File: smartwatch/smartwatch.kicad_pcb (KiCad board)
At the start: 4 copper layers, 40.1 x 29.7 mm, 35 parts, among them J1 BAT_CON, J2 DC_CON, J3 PROG_INT, J4 Screen, J5 Touch, J6 Power, SW1 SW_Push, U1 ESP32-WROVER-E, U2 MCP73831-5-OT, U3 MPU-6050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

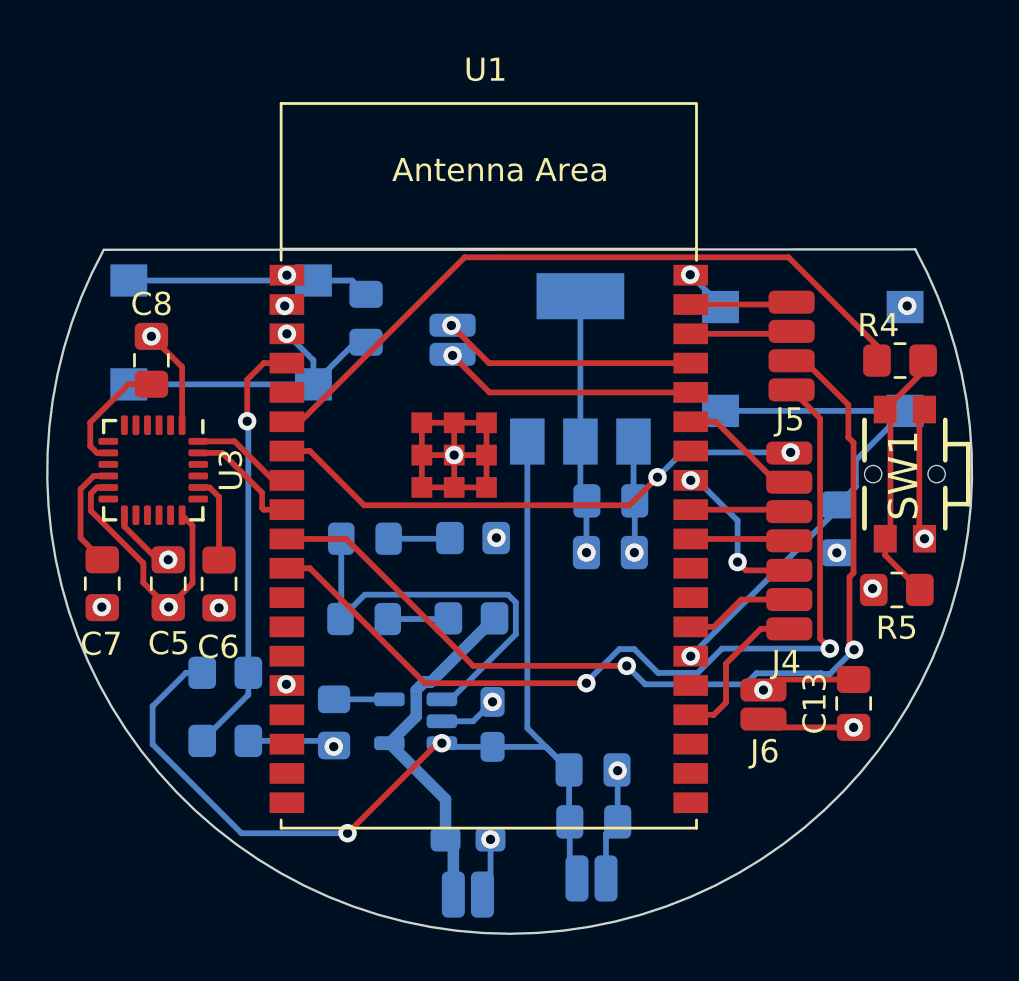
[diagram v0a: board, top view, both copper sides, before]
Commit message: added missing pullups
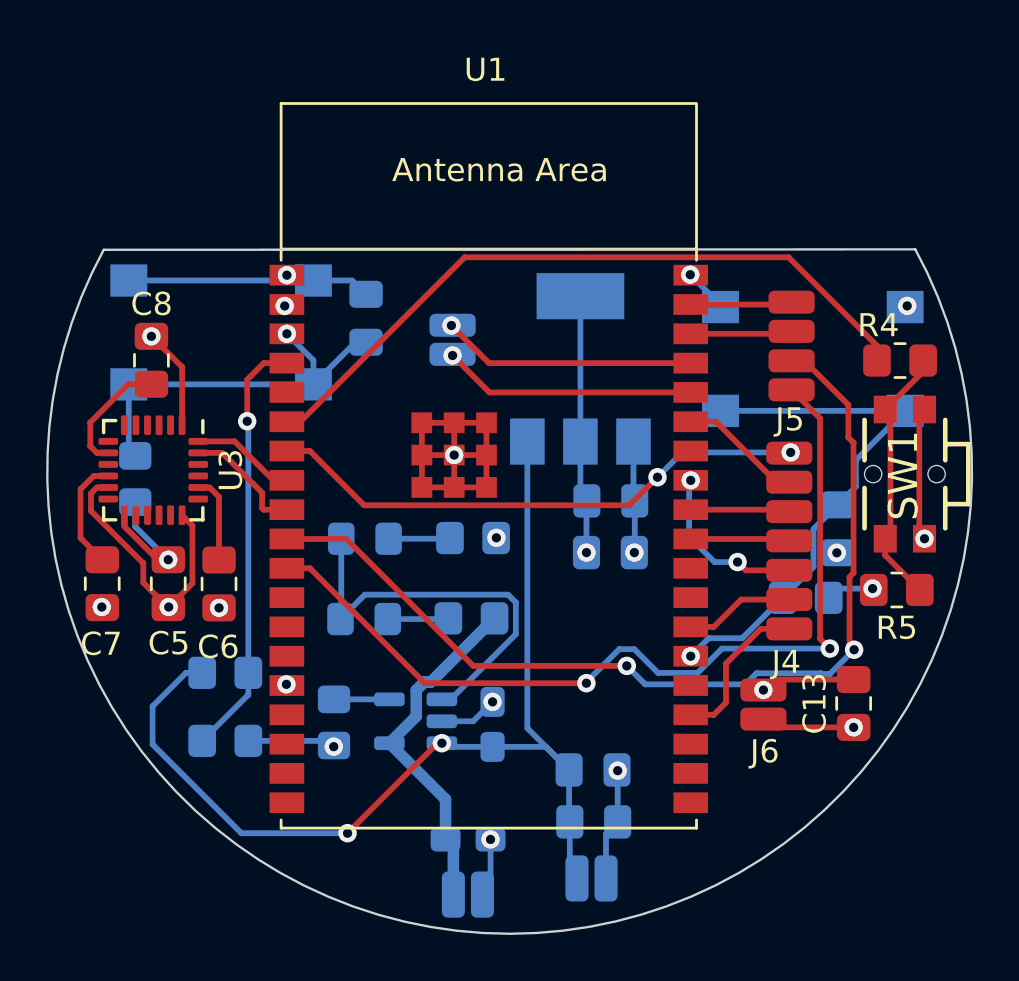
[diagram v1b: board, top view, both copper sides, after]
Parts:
- added R8: 10KΩ, Resistor_SMD:R_0805_2012Metric_Pad1.20x1.40mm_HandSolder, B.Cu at (58.4, 48.0)
- added R9: 10KΩ, Resistor_SMD:R_0805_2012Metric_Pad1.20x1.40mm_HandSolder, B.Cu at (29.3, 42.8)
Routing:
- net 3V3: track 18.5 -> 23.7 mm
- net EN: track 13.7 -> 16.9 mm
- net IO0: track 22.5 -> 23.3 mm
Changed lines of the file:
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@@
+    )
+  )
+  (footprint "Resistor_SMD:R_0805_2012Metric_Pad1.20x1.40mm_HandSolder" (layer "B.Cu")
+    (at 29.3 42.8 -90)
+    (descr "Resistor SMD 0805 (2012 Metric), square (rectangular) end terminal, IPC_7351 nominal with elongated pad for handsoldering. (Body size source: IPC-SM-782 page 72, https://www.pcb-3d.com/wordpress/wp-content/uploads/ipc-sm-782a_amendment_1_and_2.pdf), generated with kicad-footprint-generator")
+    (tags "resistor handsolder")
+    (property "Sheetfile" "smartwatch.kicad_sch")
+    (property "Sheetname" "")
+    (property "ki_description" "Resistor")
+    (property "ki_keywords" "R res resistor")
+    (attr smd)
+    (fp_text reference "R9" (at 0 1.65 90) (layer "B.SilkS")
+        (effects (font (size 1 1) (thickness 0.15)) (justify mirror))
+    )
+    (fp_text value "10KΩ" (at 0 -1.65 90) (layer "B.Fab")
+        (effects (font (size 1 1) (thickness 0.15)) (justify mirror))
+    )
+    (fp_text user "${REFERENCE}" (at 0 0 90) (layer "B.Fab")
+        (effects (font (size 0.5 0.5) (thickness 0.08)) (justify mirror))
+    )
+    (fp_line (start -0.227064 -0.735) (end 0.227064 -0.735)
+      (stroke (width 0.12) (type solid)) (layer "B.SilkS"))
+    (fp_line (start -0.227064 0.735) (end 0.227064 0.735)
+      (stroke (width 0.12) (type solid)) (layer "B.SilkS"))
+    (fp_line (start -1.85 -0.95) (end -1.85 0.95)
+      (stroke (width 0.05) (type solid)) (layer "B.CrtYd"))
+    (fp_line (start -1.85 0.95) (end 1.85 0.95)
+      (stroke (width 0.05) (type solid)) (layer "B.CrtYd"))
+    (fp_line (start 1.85 -0.95) (end -1.85 -0.95)
+      (stroke (width 0.05) (type solid)) (layer "B.CrtYd"))
+    (fp_line (start 1.85 0.95) (end 1.85 -0.95)
+      (stroke (width 0.05) (type solid)) (layer "B.CrtYd"))
+    (fp_line (start -1 -0.625) (end -1 0.625)
+      (stroke (width 0.1) (type solid)) (layer "B.Fab"))
+    (fp_line (start -1 0.625) (end 1 0.625)
+      (stroke (width 0.1) (type solid)) (layer "B.Fab"))
+    (fp_line (start 1 -0.625) (end -1 -0.625)
+      (stroke (width 0.1) (type solid)) (layer "B.Fab"))
+    (fp_line (start 1 0.625) (end 1 -0.625)
+      (stroke (width 0.1) (type solid)) (layer "B.Fab"))
+    (pad "1" smd roundrect (at -1 0 270) (size 1.2 1.4) (layers "B.Cu" "B.Paste" "B.Mask") (roundrect_rratio 0.208333)
+      (net 8 "EN") (pintype "passive"))
+    (pad "2" smd roundrect (at 1 0 270) (size 1.2 1.4) (layers "B.Cu" "B.Paste" "B.Mask") (roundrect_rratio 0.208333)
+      (net 4 "3V3") (pintype "passive"))
+    (model "${KICAD6_3DMODEL_DIR}/Resistor_SMD.3dshapes/R_0805_2012Metric.wrl"
+      (offset (xyz 0 0 0))
+      (scale (xyz 1 1 1))
+      (rotate (xyz 0 0 0))
     )
   )
@@
     )
   )
+  (footprint "Resistor_SMD:R_0805_2012Metric_Pad1.20x1.40mm_HandSolder" (layer "B.Cu")
+    (at 58.35 47.95 180)
+    (descr "Resistor SMD 0805 (2012 Metric), square (rectangular) end terminal, IPC_7351 nominal with elongated pad for handsoldering. (Body size source: IPC-SM-782 page 72, https://www.pcb-3d.com/wordpress/wp-content/uploads/ipc-sm-782a_amendment_1_and_2.pdf), generated with kicad-footprint-generator")
+    (tags "resistor handsolder")
+    (property "Sheetfile" "smartwatch.kicad_sch")
+    (property "Sheetname" "")
+    (property "ki_description" "Resistor")
+    (property "ki_keywords" "R res resistor")
+    (attr smd)
+    (fp_text reference "R8" (at -0.05 -1.75) (layer "B.SilkS")
+        (effects (font (size 1 1) (thickness 0.15)) (justify mirror))
+    )
+    (fp_text value "10KΩ" (at 0 -1.65) (layer "B.Fab")
+        (effects (font (size 1 1) (thickness 0.15)) (justify mirror))
+    )
+    (fp_text user "${REFERENCE}" (at 0 0) (layer "B.Fab")
+        (effects (font (size 0.5 0.5) (thickness 0.08)) (justify mirror))
+    )
+    (fp_line (start -0.227064 -0.735) (end 0.227064 -0.735)
+      (stroke (width 0.12) (type solid)) (layer "B.SilkS"))
+    (fp_line (start -0.227064 0.735) (end 0.227064 0.735)
+      (stroke (width 0.12) (type solid)) (layer "B.SilkS"))
+    (fp_line (start -1.85 -0.95) (end -1.85 0.95)
+      (stroke (width 0.05) (type solid)) (layer "B.CrtYd"))
+    (fp_line (start -1.85 0.95) (end 1.85 0.95)
+      (stroke (width 0.05) (type solid)) (layer "B.CrtYd"))
+    (fp_line (start 1.85 -0.95) (end -1.85 -0.95)
+      (stroke (width 0.05) (type solid)) (layer "B.CrtYd"))
+    (fp_line (start 1.85 0.95) (end 1.85 -0.95)
+      (stroke (width 0.05) (type solid)) (layer "B.CrtYd"))
+    (fp_line (start -1 -0.625) (end -1 0.625)
+      (stroke (width 0.1) (type solid)) (layer "B.Fab"))
+    (fp_line (start -1 0.625) (end 1 0.625)
+      (stroke (width 0.1) (type solid)) (layer "B.Fab"))
+    (fp_line (start 1 -0.625) (end -1 -0.625)
+      (stroke (width 0.1) (type solid)) (layer "B.Fab"))
+    (fp_line (start 1 0.625) (end 1 -0.625)
+      (stroke (width 0.1) (type solid)) (layer "B.Fab"))
+    (pad "1" smd roundrect (at -1 0 180) (size 1.2 1.4) (layers "B.Cu" "B.Paste" "B.Mask") (roundrect_rratio 0.208333)
+      (net 4 "3V3") (pintype "passive"))
+    (pad "2" smd roundrect (at 1 0 180) (size 1.2 1.4) (layers "B.Cu" "B.Paste" "B.Mask") (roundrect_rratio 0.208333)
+      (net 1 "IO0") (pintype "passive"))
+    (model "${KICAD6_3DMODEL_DIR}/Resistor_SMD.3dshapes/R_0805_2012Metric.wrl"
+      (offset (xyz 0 0 0))
+      (scale (xyz 1 1 1))
+      (rotate (xyz 0 0 0))
+    )
+  )
   (footprint "Capacitor_SMD:C_0805_2012Metric_Pad1.18x1.45mm_HandSolder" (layer "B.Cu")
     (at 49.1675 57.66 180)
@@
   (via (at 53.37 50.48) (size 0.8) (drill 0.4) (layers "F.Cu" "B.Cu") (net 1))
   (segment (start 62.66 39.85) (end 54.66 39.85) (width 0.25) (layer "B.Cu") (net 1))
+  (segment (start 55.6 49.7) (end 54.15 49.7) (width 0.25) (layer "B.Cu") (net 1))
   (segment (start 60.525 43.1375) (end 59.74 43.9225) (width 0.25) (layer "B.Cu") (net 1))
+  (segment (start 54.15 49.7) (end 53.37 50.48) (width 0.25) (layer "B.Cu") (net 1))
+  (segment (start 58.69 44.9725) (end 58.69 46.61) (width 0.25) (layer "B.Cu") (net 1))
   (segment (start 60.525 41.985) (end 60.525 43.1375) (width 0.25) (layer "B.Cu") (net 1))
-  (segment (start 59.74 43.9225) (end 59.74 44.11) (width 0.25) (layer "B.Cu") (net 1))
-  (segment (start 59.74 44.11) (end 53.37 50.48) (width 0.25) (layer "B.Cu") (net 1))
+  (segment (start 58.69 46.61) (end 55.6 49.7) (width 0.25) (layer "B.Cu") (net 1))
+  (segment (start 59.74 43.9225) (end 58.69 44.9725) (width 0.25) (layer "B.Cu") (net 1))
   (segment (start 62.66 39.85) (end 60.525 41.985) (width 0.25) (layer "B.Cu") (net 1))
   (segment (start 35.87 51.72) (end 35.85 51.7) (width 0.25) (layer "F.Cu") (net 2))
@@
   (via (at 35.776405 35.303268) (size 0.8) (drill 0.4) (layers "F.Cu" "B.Cu") (net 4))
   (via (at 48.8525 45.99) (size 0.8) (drill 0.4) (layers "F.Cu" "B.Cu") (net 4))
+  (segment (start 59.75 47.55) (end 59.35 47.95) (width 0.25) (layer "B.Cu") (net 4))
+  (segment (start 29.3 44.87) (end 30.73 46.3) (width 0.25) (layer "B.Cu") (net 4))
+  (segment (start 61.25 47.55) (end 59.75 47.55) (width 0.25) (layer "B.Cu") (net 4))
   (segment (start 48.59 41.18) (end 48.59 34.88) (width 0.25) (layer "B.Cu") (net 4))
   (segment (start 48.59 41.18) (end 48.59 43.47) (width 0.25) (layer "B.Cu") (net 4))
@@
   (segment (start 48.8525 43.7675) (end 48.87 43.75) (width 0.25) (layer "B.Cu") (net 4))
   (segment (start 48.8525 45.99) (end 48.8525 43.7675) (width 0.25) (layer "B.Cu") (net 4))
+  (segment (start 29.3 43.8) (end 29.3 44.87) (width 0.25) (layer "B.Cu") (net 4))
   (segment (start 32.520685 43.17) (end 32.93 43.579315) (width 0.25) (layer "F.Cu") (net 5))
   (segment (start 32.03 43.17) (end 32.520685 43.17) (width 0.25) (layer "F.Cu") (net 5))
@@
   (via (at 35.87 36.51) (size 0.8) (drill 0.4) (layers "F.Cu" "B.Cu") (net 8))
   (segment (start 39.3 36.875) (end 38.845 36.875) (width 0.25) (layer "B.Cu") (net 8))
+  (segment (start 29.02 38.7) (end 29.02 41.52) (width 0.25) (layer "B.Cu") (net 8))
   (segment (start 29.02 38.7) (end 37.02 38.7) (width 0.25) (layer "B.Cu") (net 8))
   (segment (start 37.02 38.7) (end 37.02 37.66) (width 0.25) (layer "B.Cu") (net 8))
   (segment (start 37.02 37.66) (end 35.87 36.51) (width 0.25) (layer "B.Cu") (net 8))
   (segment (start 38.845 36.875) (end 37.02 38.7) (width 0.25) (layer "B.Cu") (net 8))
+  (segment (start 29.02 41.52) (end 29.3 41.8) (width 0.25) (layer "B.Cu") (net 8))
   (segment (start 41.475 51.951472) (end 41.826472 51.6) (width 0.5) (layer "B.Cu") (net 9))
   (segment (start 41.826472 51.6) (end 42.1075 51.6) (width 0.5) (layer "B.Cu") (net 9))
@@
   (via (at 55.4 46.4) (size 0.8) (drill 0.4) (layers "F.Cu" "B.Cu") (net 24))
   (via (at 53.37 42.86) (size 0.8) (drill 0.4) (layers "F.Cu" "B.Cu") (net 24))
-  (segment (start 53.65 42.85) (end 53.38 42.85) (width 0.25) (layer "B.Cu") (net 24))
-  (segment (start 55.4 46.4) (end 55.4 44.6) (width 0.25) (layer "B.Cu") (net 24))
-  (segment (start 53.38 42.85) (end 53.37 42.86) (width 0.25) (layer "B.Cu") (net 24))
-  (segment (start 55.4 44.6) (end 53.65 42.85) (width 0.25) (layer "B.Cu") (net 24))
+  (segment (start 54.4 46.4) (end 53.3 45.3) (width 0.25) (layer "B.Cu") (net 24))
+  (segment (start 53.3 42.93) (end 53.37 42.86) (width 0.25) (layer "B.Cu") (net 24))
+  (segment (start 55.4 46.4) (end 54.4 46.4) (width 0.25) (layer "B.Cu") (net 24))
+  (segment (start 53.3 45.3) (end 53.3 42.93) (width 0.25) (layer "B.Cu") (net 24))
   (segment (start 37.9125 52.35) (end 40.3125 52.35) (width 0.25) (layer "B.Cu") (net 25))
   (segment (start 40.2425 48.87) (end 42.8375 48.87) (width 0.25) (layer "B.Cu") (net 26))

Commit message: added connector
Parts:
- removed J5: Touch, Connector_Wire_SMD:Wire_Pad_1x04
- removed J6: Power, Connector_Wire_SMD:Wire_Pad_1x02
- J4: value Screen -> SM13B-GHS-TB; footprint Connector_Wire_SMD:Wire_Pad_1x07 -> SM13B-GHS-TB:JST_SM13B-GHS-TB
- R4, R5, SW1: moved to B.Cu
- moved BOOT/FLASH1 13.6 mm to (54.5, 50.5)
- moved C9 13.1 mm to (47.9, 50.4), turned to -90 degrees
- moved C13 5.09 mm to (56.8, 56.1), turned to 0 degrees
- moved R5 5.04 mm to (58.5, 44.4), turned to -90 degrees
- moved R4 4.77 mm to (58.4, 40.2), turned to 90 degrees
- moved R8 3.44 mm to (61.0, 50.2), turned to -90 degrees
- moved J4 2.29 mm to (59.7, 44.5), turned to 90 degrees
- moved SW1 0.45 mm to (63.6, 42.6), turned to -90 degrees
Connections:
- C13 pad 1: DC_GND -> 3V3
- C13 pad 2: 3V3 -> DC_GND
- J4 pad 1: SCR_MISO -> 3V3
- J4 pad 2: SCR_MOSI -> DC_GND
- J4 pad 3: SCR_SCLK -> SCR_MISO
- J4 pad 4: SCR_CS -> SCR_MOSI
- J4 pad 5: SCR_DC -> SCR_SCLK
- J4 pad 6: SCR_RST -> SCR_CS
- J4 pad 7: SCR_BL -> SCR_DC
- R6 pad 1: BAT_MEASURE -> BAT_VDD
- R6 pad 2: BAT_VDD -> BAT_MEASURE
- R7 pad 1: DC_GND -> BAT_MEASURE
- R7 pad 2: BAT_MEASURE -> DC_GND
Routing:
- net DC_GND: track 75.6 -> 92.8 mm, vias 18 -> 16
- net TOUCH_IRQ: track 41.9 -> 25.5 mm, vias 2 -> 4
- net TOUCH_RST: track 39.0 -> 27.6 mm, vias 2 -> 4
- net SCR_BL: track 6.80 -> 17.0 mm, vias 0 -> 2
- net SCR_RST: track 4.76 -> 14.9 mm, vias 0 -> 2
- net IO0: track 23.3 -> 15.1 mm, vias 1 -> 0
- net TOUCH_SDA: track 4.41 -> 11.5 mm
- net Net-(R4-Pad1): track 11.4 -> 17.0 mm
- net SCR_MOSI: track 5.36 -> 9.96 mm, vias 0 -> 2
- net SCR_DC: track 7.41 -> 3.81 mm, vias 2 -> 0
- net BTN_INP: track 30.8 -> 34.2 mm, vias 0 -> 1
- net BAT_VDD: track 46.0 -> 44.0 mm
- net SCR_CS: track 4.30 -> 3.27 mm
- net SCR_MISO: track 23.8 -> 24.7 mm
- net BAT_MEASURE: track 18.5 -> 19.4 mm
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
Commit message: finished routing
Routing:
- net IO0: track 15.1 -> 18.9 mm, vias 0 -> 1
- net DC_GND: track 92.8 -> 92.9 mm, vias 16 -> 17
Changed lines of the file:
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@@
   (gr_line (start 27.935217 32.869223) (end 63.1 32.85)
     (stroke (width 0.1) (type default)) (layer "Edge.Cuts"))
+  (via (at 53.37 50.48) (size 0.8) (drill 0.4) (layers "F.Cu" "B.Cu") (net 1))
   (segment (start 60.95 51.2) (end 59.35 52.8) (width 0.25) (layer "B.Cu") (net 1))
+  (segment (start 50.55 52.8) (end 52.87 50.48) (width 0.25) (layer "B.Cu") (net 1))
   (segment (start 59.35 52.8) (end 58.55 52.8) (width 0.25) (layer "B.Cu") (net 1))
   (segment (start 47.85 51.4375) (end 49.2125 52.8) (width 0.25) (layer "B.Cu") (net 1))
+  (segment (start 52.87 50.48) (end 53.37 50.48) (width 0.25) (layer "B.Cu") (net 1))
   (segment (start 50.55 52.8) (end 51.495 53.745) (width 0.25) (layer "B.Cu") (net 1))
   (segment (start 49.2125 52.8) (end 50.55 52.8) (width 0.25) (layer "B.Cu") (net 1))
@@
   (via (at 35.87 33.97) (size 0.8) (drill 0.4) (layers "F.Cu" "B.Cu") (net 2))
   (via (at 35.85 51.7) (size 0.8) (drill 0.4) (layers "F.Cu" "B.Cu") (net 2))
+  (via (at 32.258 54.102) (size 0.8) (drill 0.4) (layers "F.Cu" "B.Cu") (net 2))
   (via (at 43.12 41.765) (size 0.8) (drill 0.4) (layers "F.Cu" "B.Cu") (net 2))
   (segment (start 50.55 48.3) (end 48.9125 48.3) (width 0.25) (layer "B.Cu") (net 2))
@@
   (segment (start 44.94 45.36) (end 44.95 45.35) (width 0.25) (layer "B.Cu") (net 2))
   (segment (start 44.7825 52.46) (end 43.9425 53.3) (width 0.25) (layer "B.Cu") (net 2))
+  (segment (start 32.21 54.15) (end 32.258 54.102) (width 0.25) (layer "B.Cu") (net 2))
   (segment (start 39.3 34.8) (end 38.7 34.2) (width 0.25) (layer "B.Cu") (net 2))
   (segment (start 58.55 48.3) (end 59.786827 47.063173) (width 0.25) (layer "B.Cu") (net 2))
@@
   (segment (start 48.9125 48.3) (end 47.85 49.3625) (width 0.25) (layer "B.Cu") (net 2))
   (segment (start 49.7 58.165) (end 50.205 57.66) (width 0.25) (layer "B.Cu") (net 2))
+  (segment (start 32.2 54.15) (end 32.21 54.15) (width 0.25) (layer "B.Cu") (net 2))
   (segment (start 38.7 34.2) (end 37.02 34.2) (width 0.25) (layer "B.Cu") (net 2))
   (segment (start 44.9375 45.36) (end 44.94 45.36) (width 0.25) (layer "B.Cu") (net 2))
@@
   (via (at 56.45 49.55) (size 0.8) (drill 0.4) (layers "F.Cu" "B.Cu") (net 17))
   (via (at 50.15 50.4) (size 0.8) (drill 0.4) (layers "F.Cu" "B.Cu") (net 17))
-  (segment (start 56.45 49.55) (end 56.45 49.7) (width 0.25) (layer "B.Cu") (net 17))
-  (segment (start 56.45 49.7) (end 55.75 50.4) (width 0.25) (layer "B.Cu") (net 17))
-  (segment (start 55.75 50.4) (end 50.15 50.4) (width 0.25) (layer "B.Cu") (net 17))
+  (segment (start 56.45 49.55) (end 56.43 49.53) (width 0.25) (layer "B.Cu") (net 17))
+  (segment (start 56.43 49.53) (end 51.02 49.53) (width 0.25) (layer "B.Cu") (net 17))
+  (segment (start 51.02 49.53) (end 50.15 50.4) (width 0.25) (layer "B.Cu") (net 17))
   (segment (start 56.55 48.25) (end 56.6 48.3) (width 0.25) (layer "F.Cu") (net 18))
   (segment (start 56.5 48.25) (end 56.55 48.25) (width 0.25) (layer "F.Cu") (net 18))
